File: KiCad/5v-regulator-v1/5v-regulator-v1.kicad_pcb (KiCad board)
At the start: 2 copper layers, 105.3 x 47.5 mm, 42 parts, among them J1 Screw_Terminal_01x02, J2 USB-A1SSW6, J3 USB-A1SSW6, J4 USB-A1SSW6, J5 USB-A1SSW6, J6 Screw_Terminal_01x04, Q1 Q_Dual_NMOS_S1G1D2S2G2D1, SW1 SW_SPST, U1 TPS51386RJNR, U2 INA219AIDR, U3 INA219AIDR

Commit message: Updated PCB design
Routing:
- net GND: track 40.1 -> 36.1 mm
- net Net-(J5-D+): track 0.00 -> 2.00 mm
- net Net-(J3-D+): track 0.00 -> 2.00 mm
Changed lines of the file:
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@@
 		(tags "LED handsolder")
 		(property "Reference" "D2"
-			(at 0 -1.65 270)
+			(at 0 -1.65 -90)
 			(layer "F.SilkS")
 			(effects
@@
 		)
 		(property "Value" "LED"
-			(at 0 1.65 270)
+			(at 0 1.65 -90)
 			(layer "F.Fab")
 			(effects
@@
 		)
 		(fp_text user "${REFERENCE}"
-			(at 0 0 270)
+			(at 0 0 -90)
 			(layer "F.Fab")
 			(effects
@@
 		)
 		(fp_text user "${REFERENCE}"
-			(at 0 0 360)
+			(at 0 0 0)
 			(layer "F.Fab")
 			(effects
@@
 		(tags "resistor handsolder")
 		(property "Reference" "R7"
-			(at 0 -1.65 360)
+			(at 0 -1.65 0)
 			(layer "F.SilkS")
 			(effects
@@
 		)
 		(property "Value" "10K"
-			(at 0 1.65 360)
+			(at 0 1.65 0)
 			(layer "F.Fab")
 			(effects
@@
 		)
 		(fp_text user "${REFERENCE}"
-			(at 0 0 360)
+			(at 0 0 0)
 			(layer "F.Fab")
 			(effects
@@
 		(at 187.111364 60.883422 165)
 		(property "Reference" "J2"
-			(at 0.16 14.4675 345)
+			(at 0.16 14.4675 -15)
 			(layer "F.SilkS")
 			(effects
@@
 		)
 		(property "Value" "USB-A1SSW6"
-			(at 7.62 13.359 345)
+			(at 7.62 13.359 -15)
 			(layer "F.Fab")
 			(effects
@@
 		(tags "LED handsolder")
 		(property "Reference" "D1"
-			(at 0 -1.65 270)
+			(at 0 -1.65 -90)
 			(layer "F.SilkS")
 			(effects
@@
 		)
 		(property "Value" "LED"
-			(at 0 1.65 270)
+			(at 0 1.65 -90)
 			(layer "F.Fab")
 			(effects
@@
 		)
 		(fp_text user "${REFERENCE}"
-			(at 0 0 270)
+			(at 0 0 -90)
 			(layer "F.Fab")
 			(effects
@@
 	)
 	(segment
-		(start 189.960201 64.747125)
-		(end 189.960201 63.332912)
+		(start 186.076088 63.332912)
+		(end 186.593726 62.815274)
 		(width 0.2)
 		(layer "B.Cu")
@@
 	)
 	(segment
-		(start 189.960201 63.332912)
-		(end 190.477839 62.815274)
+		(start 186.076088 64.747125)
+		(end 186.076088 63.332912)
 		(width 0.2)
 		(layer "B.Cu")
@@
 	)
 	(segment
+		(start 196.542674 63.573214)
+		(end 197.956887 62.159001)
+		(width 0.2)
+		(layer "B.Cu")
+		(net 7)
+	)
+	(segment
+		(start 196.562806 74.926787)
+		(end 197.977019 76.341)
+		(width 0.2)
+		(layer "B.Cu")
+		(net 8)
+	)
+	(segment
 		(start 157 56.475)
 		(end 159.975 56.475)
@@
 	)
 	(segment
-		(start 200.426787 63.573214)
-		(end 201.841 62.159001)
-		(width 0.2)
-		(layer "B.Cu")
-		(net 14)
-	)
-	(segment
-		(start 200.446919 74.926787)
-		(end 201.861132 76.341)
-		(width 0.2)
-		(layer "B.Cu")
-		(net 14)
-	)
-	(segment
 		(start 170.975 56.475)
 		(end 171 56.5)
@@
 	)
 	(segment
-		(start 189.960201 75.810853)
-		(end 190.477839 76.328491)
+		(start 186.076088 75.810853)
+		(end 186.593726 76.328491)
 		(width 0.2)
 		(layer "B.Cu")
@@
 	)
 	(segment
-		(start 189.960201 74.39664)
-		(end 189.960201 75.810853)
+		(start 186.076088 74.39664)
+		(end 186.076088 75.810853)
 		(width 0.2)
 		(layer "B.Cu")
@@
 		(polygon
 			(pts
-				(xy 148 67.5) (xy 148 62) (xy 149 62) (xy 149 62) (xy 153 62) (xy 153 71) (xy 151.5 73) (xy 147 72)
-				(xy 146 71) (xy 146 70.5) (xy 146 69) (xy 144.993699 68) (xy 147 67.5)
+				(xy 148 67.5) (xy 148 62) (xy 149 62) (xy 153 62) (xy 153 71) (xy 151.5 73) (xy 147 72) (xy 146 71)
+				(xy 146 70.5) (xy 146 69) (xy 144.993699 68) (xy 147 67.5)
 			)
 		)
@@
 		(polygon
 			(pts
-				(xy 145.5 68) (xy 146.5 59.5) (xy 148.5 59.5) (xy 148.5 61.5) (xy 148 61.5) (xy 148 67.5)
+				(xy 145.5 68) (xy 146.5 59.5) (xy 148.5 59.5) (xy 148.5 61.5) (xy 148.25 61.75) (xy 148 67.5)
 			)
 		)

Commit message: Blaine review
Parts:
- added J7: Conn_01x04_Pin, Connector_PinHeader_2.54mm:PinHeader_1x04_P2.54mm_Vertical, F.Cu at (165.1, 88.8)
- added R11: 10K, Resistor_SMD:R_0805_2012Metric_Pad1.20x1.40mm_HandSolder, F.Cu at (173.5, 87.5)
- added R12: 10K, Resistor_SMD:R_0805_2012Metric_Pad1.20x1.40mm_HandSolder, F.Cu at (169.8, 87.5)
- J2, J3, J4, J5: footprint Vertical USB:ONSHORE_USB-A1SSW6 -> Connector_USB:USB_A_Wuerth_614004134726_Horizontal
- moved J2 0.25 mm to (187.1, 60.6), turned to -105 degrees
- moved J4 0.25 mm to (187.1, 78.0), turned to 105 degrees
- turned J3 to -135 degrees
- turned J5 to 135 degrees
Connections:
- J6 pad 2: VOUT2 -> GND
- J6 pad 3: GND -> VOUT2
- Q1 pad 5: Net-(Q1B-G) -> VBATT
- R7 pad 1: Net-(Q1B-G) -> VBATT
- U2 pad 7: VIN -> unconnected-(U2-VIN--Pad7)
- U2 pad 8: VBATT -> unconnected-(U2-VIN+-Pad8)
- U3 pad 7: VOUT2 -> unconnected-(U3-VIN--Pad7)
- U3 pad 8: VOUT -> unconnected-(U3-VIN+-Pad8)
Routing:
- net Net-(J7-Pin_3): track 54.5 -> 61.1 mm
- net VOUT2: track 81.7 -> 88.2 mm
- net Net-(J7-Pin_4): track 56.4 -> 61.8 mm
- net VBATT: track 7.64 -> 10.5 mm
- net Net-(Q1B-G): track 2.88 -> 0.00 mm

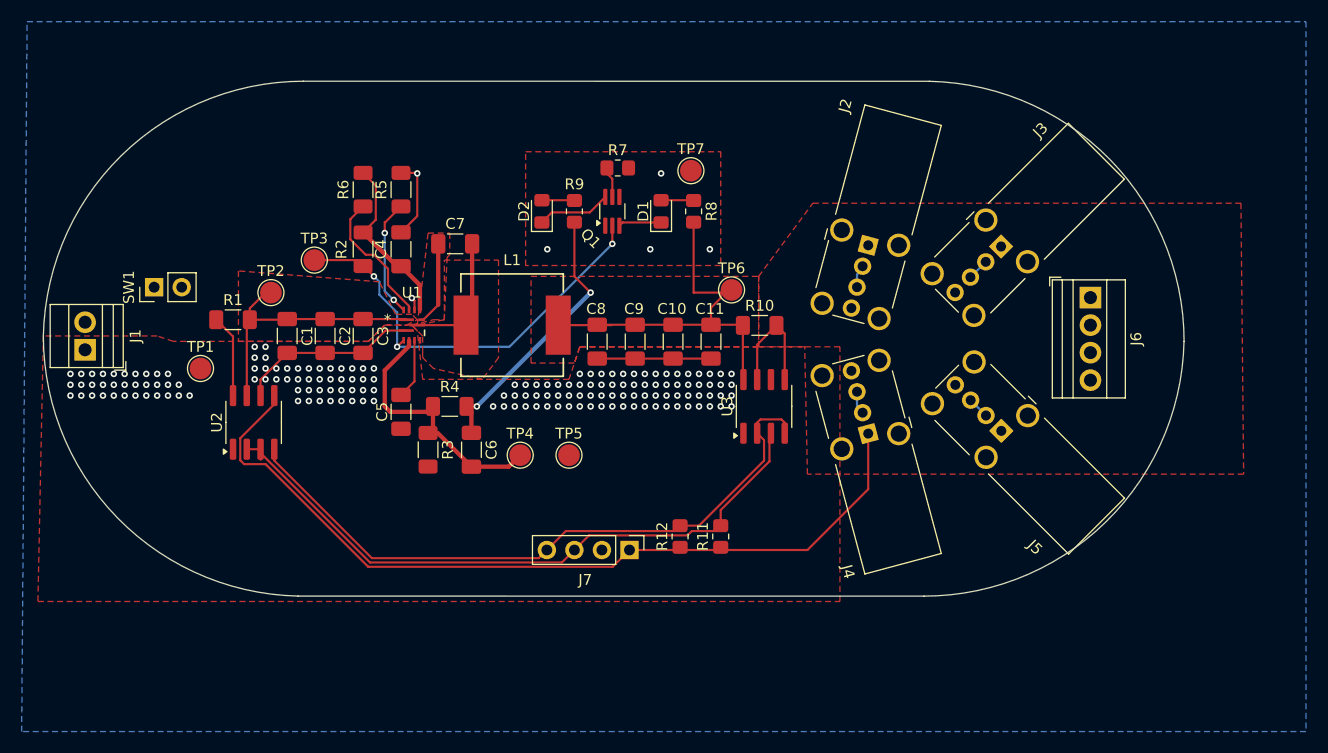
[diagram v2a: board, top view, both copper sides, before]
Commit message: Updated 5V reg and added battery meter
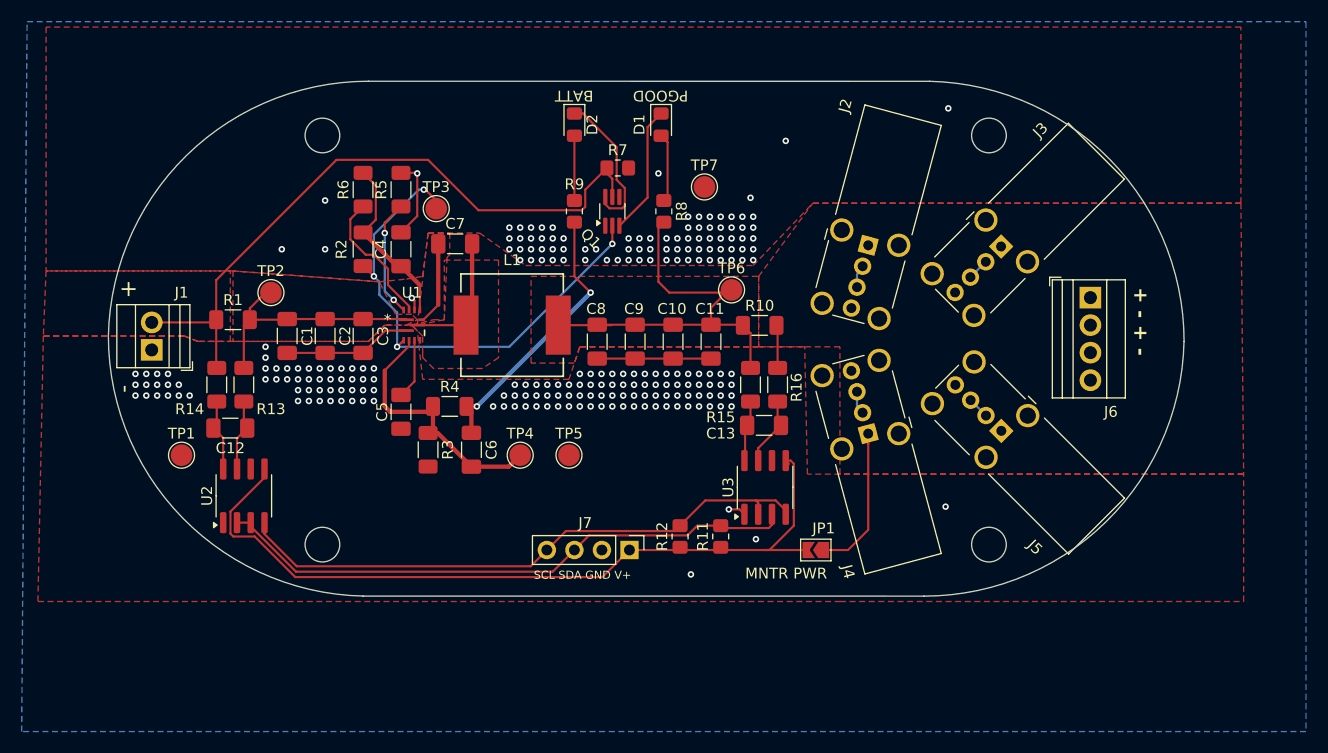
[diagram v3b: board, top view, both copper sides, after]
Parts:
- removed SW1: SW_SPST, Connector_PinHeader_2.54mm:PinHeader_1x02_P2.54mm_Vertical
- added C12: 0.1uF, Capacitor_SMD:C_1206_3216Metric_Pad1.33x1.80mm_HandSolder, F.Cu at (128.2, 77.5)
- added C13: 0.1uF, Capacitor_SMD:C_1206_3216Metric_Pad1.33x1.80mm_HandSolder, F.Cu at (177.5, 77.2)
- added JP1: SolderJumper_2_Open, Jumper:SolderJumper-2_P1.3mm_Open_TrianglePad1.0x1.5mm, F.Cu at (182.3, 88.8)
- added R13: 10, Resistor_SMD:R_1206_3216Metric_Pad1.30x1.75mm_HandSolder, F.Cu at (129.5, 73.5)
- added R14: 10, Resistor_SMD:R_1206_3216Metric_Pad1.30x1.75mm_HandSolder, F.Cu at (127.0, 73.5)
- added R15: 10, Resistor_SMD:R_1206_3216Metric_Pad1.30x1.75mm_HandSolder, F.Cu at (176.2, 73.5)
- added R16: 10, Resistor_SMD:R_1206_3216Metric_Pad1.30x1.75mm_HandSolder, F.Cu at (178.8, 73.5)
- added REF**: MountingHole_3.2mm_M3, MountingHole:MountingHole_3.2mm_M3, F.Cu at (198.2, 88.2)
- added REF**: MountingHole_3.2mm_M3, MountingHole:MountingHole_3.2mm_M3, F.Cu at (136.8, 50.5)
- added REF**: MountingHole_3.2mm_M3, MountingHole:MountingHole_3.2mm_M3, F.Cu at (198.2, 50.5)
- added REF**: MountingHole_3.2mm_M3, MountingHole:MountingHole_3.2mm_M3, F.Cu at (136.8, 88.2)
- moved TP3 12.2 mm to (147.2, 57.2)
- moved D2 8.54 mm to (160.0, 49.5), turned to -90 degrees
- moved TP1 8.19 mm to (123.8, 80.0)
- moved D1 8.00 mm to (168.0, 49.5), turned to -90 degrees
- moved U3 7.48 mm to (177.6, 83.0)
- moved U2 6.84 mm to (129.5, 83.8)
- moved J1 6.15 mm to (121.0, 70.3)
- moved R8 2.75 mm to (168.2, 57.5)
- moved TP7 1.95 mm to (172.0, 55.2)
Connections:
- J1 pad 2: Net-(J1-Pin_2) -> VBATT
- J7 pad 1: VOUT2 -> Net-(J7-Pin_1)
- R11 pad 1: VOUT2 -> Net-(J7-Pin_1)
- R12 pad 1: VOUT2 -> Net-(J7-Pin_1)
- U2 pad 5: VOUT2 -> Net-(J7-Pin_1)
- U2 pad 7: unconnected-(U2-VIN--Pad7) -> Net-(U2-VIN-)
- U2 pad 8: unconnected-(U2-VIN+-Pad8) -> Net-(U2-VIN+)
- U3 pad 5: VOUT2 -> Net-(J7-Pin_1)
- U3 pad 7: unconnected-(U3-VIN--Pad7) -> Net-(U3-VIN-)
- U3 pad 8: unconnected-(U3-VIN+-Pad8) -> Net-(U3-VIN+)
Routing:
- net Net-(J7-Pin_1): track 0.00 -> 73.9 mm
- net VOUT2: track 88.2 -> 18.4 mm
- net VBATT: track 10.5 -> 62.6 mm
- net PGOOD: track 39.8 -> 48.4 mm, vias 3 -> 4
- net Net-(D1-K): track 3.98 -> 11.9 mm
- net Net-(D2-K): track 6.83 -> 13.6 mm
- net Net-(U2-VIN-): track 0.00 -> 6.80 mm
- net Net-(U2-VIN+): track 0.00 -> 6.78 mm
- net Net-(J7-Pin_3): track 61.1 -> 54.4 mm
- net Net-(U3-VIN-): track 0.00 -> 6.45 mm
- net Net-(J7-Pin_4): track 61.8 -> 55.5 mm
- net Net-(U3-VIN+): track 0.00 -> 5.68 mm
- net Net-(D1-A): track 3.01 -> 6.37 mm
- net GND: track 36.1 -> 32.7 mm, vias 164 -> 226
- net Net-(D2-A): track 3.01 -> 6.01 mm
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- added copper zone on F.Cu, net VBATT
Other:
- board size 105.3 x 47.5 mm -> 99.3 x 47.5 mm
- board text added: "+"
- board text added: "+ - + -"
- board text added: "-"
- board text added: "09.03.24"
- board text added: "5V DC BUCK CONVERTER"
- board text added: "BATT"
- board text added: "BUILT DIFFERENT"
- board text added: "MNTR PWR"
- board text added: "PGOOD"
- board text added: "SCL SDA GND V+"
- board text added: "V1.0"
- board text added: "Vin: 10V-26V"
